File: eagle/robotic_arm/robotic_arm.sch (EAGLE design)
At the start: 0 parts

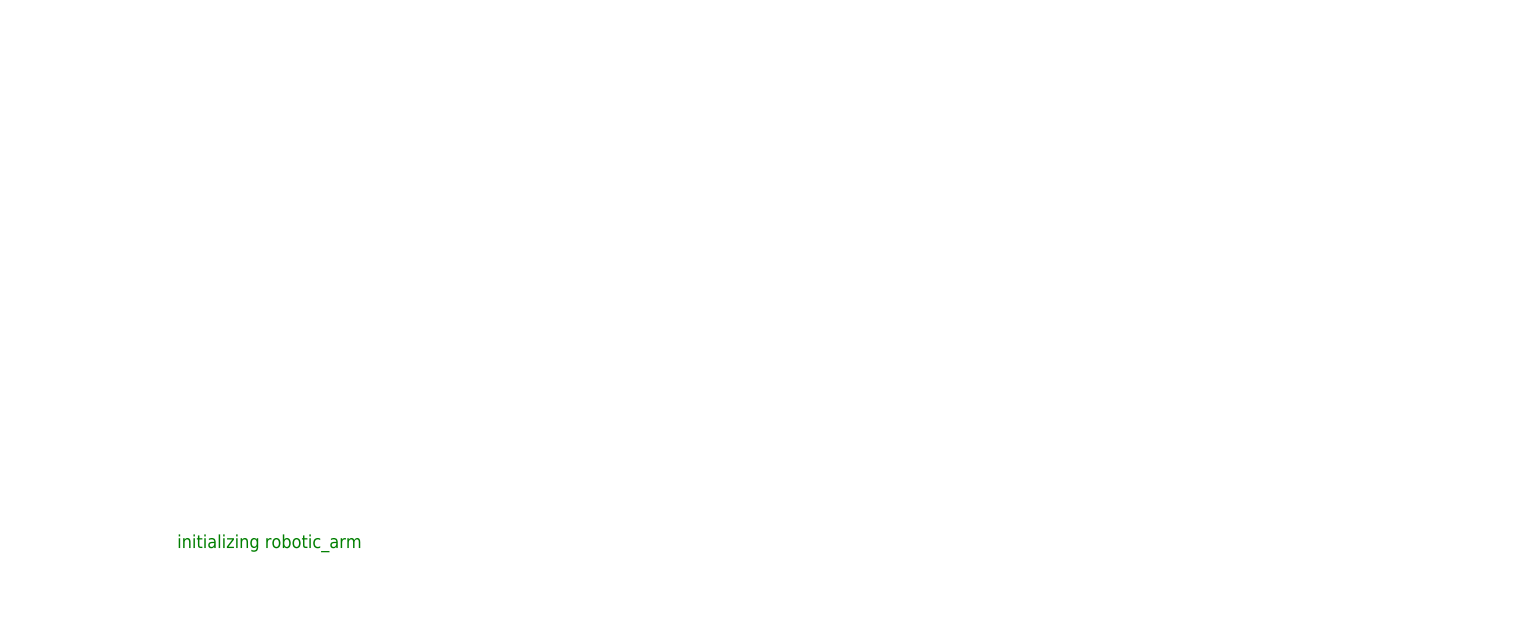
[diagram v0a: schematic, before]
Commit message: Added PWM driver and DEMUX to both robotic arm and touch glove.  Added some transistors to touch glove
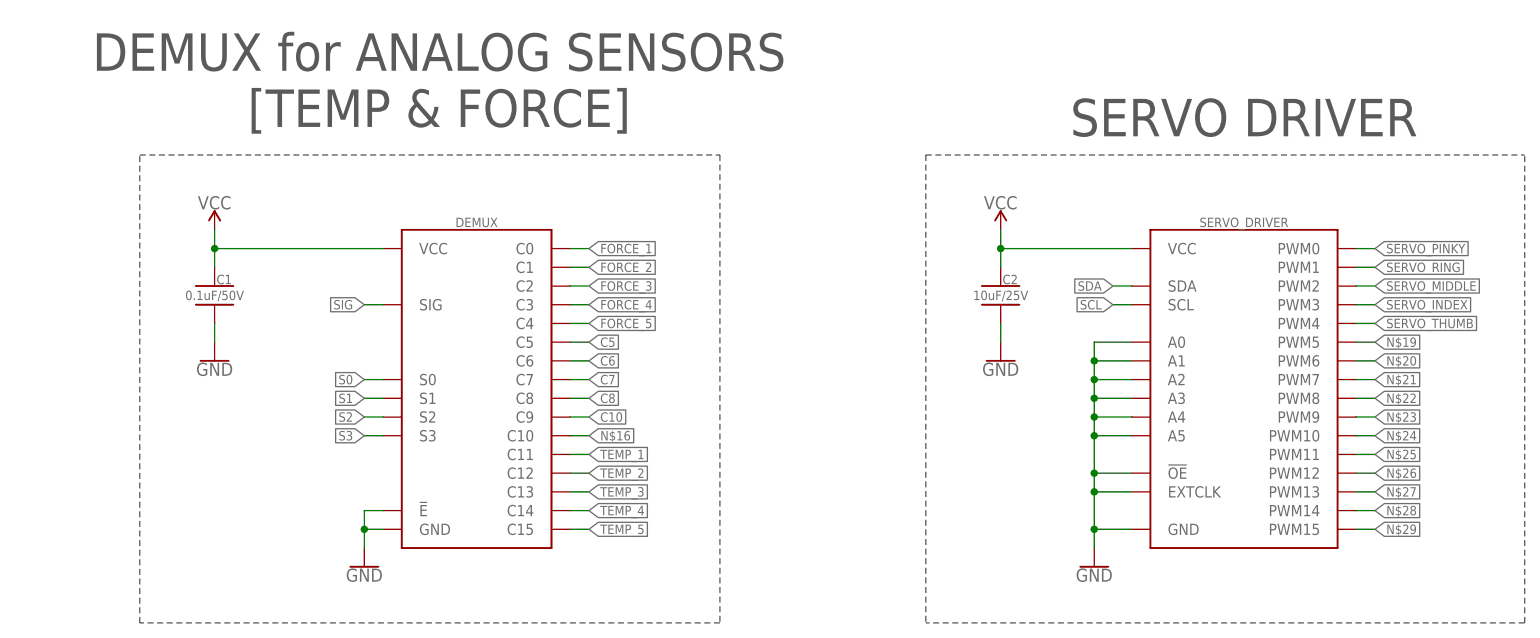
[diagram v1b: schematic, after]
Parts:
- added C1: CAP_CER_SMD-805_0.1UF-50V-10%, MrSwirlyEyes:CAP_CER_SMD-805_0.1UF-50V-10%
- added C2: CAP_CER_SMD-805_10UF-25V-10%, MrSwirlyEyes:CAP_CER_SMD-805_10UF-25V-10%
- added DEMUX: CD74HCT4067_16-CH_MUX-DEMUX, MrSwirlyEyes:CD74HCT4067_16-CH_MUX-DEMUX
- added SERVO_DRIVER: PCA9685_16-CH_12-BIT_PWM-DRIVER, MrSwirlyEyes:PCA9685_16-CH_12-BIT_PWM-DRIVER
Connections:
- new net C10: DEMUX.C9
- new net C5: DEMUX.C5
- new net C6: DEMUX.C6
- new net C7: DEMUX.C7
- new net C8: DEMUX.C8
- new net FORCE_1: DEMUX.C0
- new net FORCE_2: DEMUX.C1
- new net FORCE_3: DEMUX.C2
- new net FORCE_4: DEMUX.C3
- new net FORCE_5: DEMUX.C4
- new net GND: C1.2, C2.2, DEMUX.!E, DEMUX.GND, SERVO_DRIVER.!OE, SERVO_DRIVER.A0, SERVO_DRIVER.A1, SERVO_DRIVER.A2, SERVO_DRIVER.A3, SERVO_DRIVER.A4, SERVO_DRIVER.A5, SERVO_DRIVER.EXTCLK, SERVO_DRIVER.GND
- new net N$16: DEMUX.C10
- new net N$19: SERVO_DRIVER.PWM5
- new net N$20: SERVO_DRIVER.PWM6
- new net N$21: SERVO_DRIVER.PWM7
- new net N$22: SERVO_DRIVER.PWM8
- new net N$23: SERVO_DRIVER.PWM9
- new net N$24: SERVO_DRIVER.PWM10
- new net N$25: SERVO_DRIVER.PWM11
- new net N$26: SERVO_DRIVER.PWM12
- new net N$27: SERVO_DRIVER.PWM13
- new net N$28: SERVO_DRIVER.PWM14
- new net N$29: SERVO_DRIVER.PWM15
- new net S0: DEMUX.S0
- new net S1: DEMUX.S1
- new net S2: DEMUX.S2
- new net S3: DEMUX.S3
- new net SCL: SERVO_DRIVER.SCL
- new net SDA: SERVO_DRIVER.SDA
- new net SERVO_INDEX: SERVO_DRIVER.PWM3
- new net SERVO_MIDDLE: SERVO_DRIVER.PWM2
- new net SERVO_PINKY: SERVO_DRIVER.PWM0
- new net SERVO_RING: SERVO_DRIVER.PWM1
- new net SERVO_THUMB: SERVO_DRIVER.PWM4
- new net SIG: DEMUX.SIG
- new net TEMP_1: DEMUX.C11
- new net TEMP_2: DEMUX.C12
- new net TEMP_3: DEMUX.C13
- new net TEMP_4: DEMUX.C14
- new net TEMP_5: DEMUX.C15
- new net VCC: C1.1, C2.1, DEMUX.VCC, SERVO_DRIVER.VCC
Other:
- note added: "DEMUX for ANALOG SENSORS [TEMP & FORCE]"
- note added: "SERVO DRIVER"
- note removed: "initializing robotic_arm"

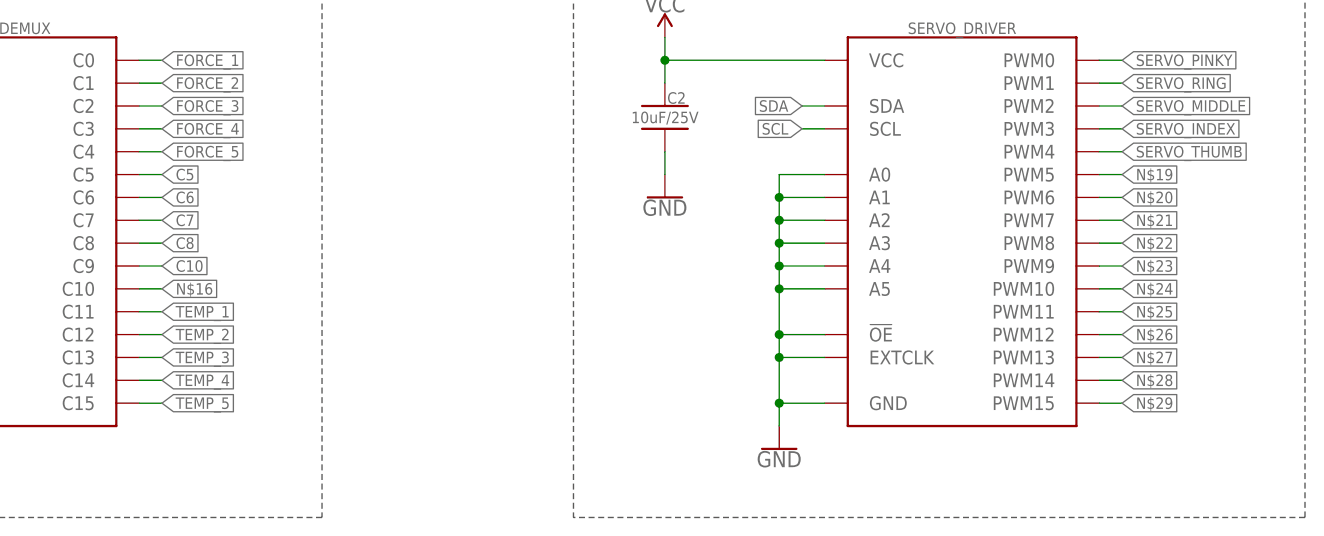
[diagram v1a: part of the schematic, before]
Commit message: Added vibe motor plus transistor driver arrangement
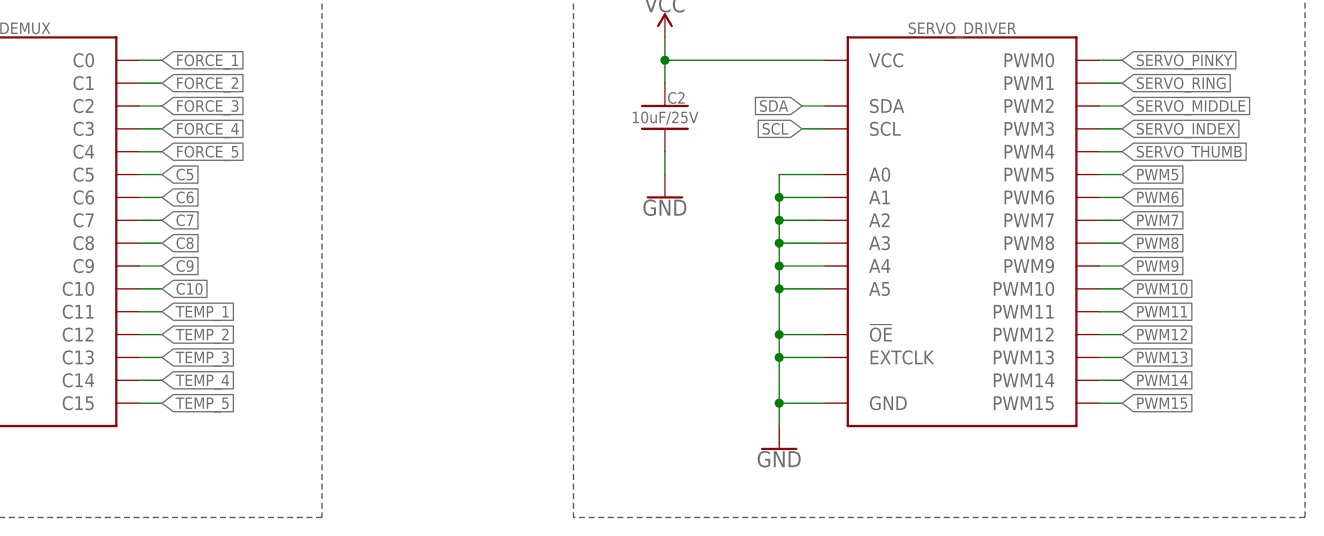
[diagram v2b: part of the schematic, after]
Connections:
- net N$19 renamed PWM5
- net N$20 renamed PWM6
- net N$21 renamed PWM7
- net N$22 renamed PWM8
- net N$23 renamed PWM9
- net N$24 renamed PWM10
- net N$25 renamed PWM11
- net N$26 renamed PWM12
- net N$27 renamed PWM13
- net N$28 renamed PWM14
- net N$29 renamed PWM15
- removed net N$16: DEMUX.C10
- new net C9: DEMUX.C9
- net C10: now also DEMUX.C10; no longer DEMUX.C9
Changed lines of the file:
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@@
 </segment>
 </net>
-<net name="C10" class="0">
+<net name="C9" class="0">
 <segment>
 <pinref part="DEMUX" gate="G$1" pin="C9"/>
@@
 </segment>
 </net>
-<net name="N$16" class="0">
+<net name="C10" class="0">
 <segment>
 <pinref part="DEMUX" gate="G$1" pin="C10"/>
@@
 </segment>
 </net>
-<net name="N$19" class="0">
+<net name="PWM5" class="0">
 <segment>
 <pinref part="SERVO_DRIVER" gate="G$1" pin="PWM5"/>
@@
 </segment>
 </net>
-<net name="N$20" class="0">
+<net name="PWM6" class="0">
 <segment>
 <pinref part="SERVO_DRIVER" gate="G$1" pin="PWM6"/>
@@
 </segment>
 </net>
-<net name="N$21" class="0">
+<net name="PWM7" class="0">
 <segment>
 <pinref part="SERVO_DRIVER" gate="G$1" pin="PWM7"/>
@@
 </segment>
 </net>
-<net name="N$22" class="0">
+<net name="PWM8" class="0">
 <segment>
 <pinref part="SERVO_DRIVER" gate="G$1" pin="PWM8"/>
@@
 </segment>
 </net>
-<net name="N$23" class="0">
+<net name="PWM9" class="0">
 <segment>
 <pinref part="SERVO_DRIVER" gate="G$1" pin="PWM9"/>
@@
 </segment>
 </net>
-<net name="N$24" class="0">
+<net name="PWM10" class="0">
 <segment>
 <pinref part="SERVO_DRIVER" gate="G$1" pin="PWM10"/>
@@
 </segment>
 </net>
-<net name="N$25" class="0">
+<net name="PWM11" class="0">
 <segment>
 <pinref part="SERVO_DRIVER" gate="G$1" pin="PWM11"/>
@@
 </segment>
 </net>
-<net name="N$26" class="0">
+<net name="PWM12" class="0">
 <segment>
 <pinref part="SERVO_DRIVER" gate="G$1" pin="PWM12"/>
@@
 </segment>
 </net>
-<net name="N$27" class="0">
+<net name="PWM13" class="0">
 <segment>
 <pinref part="SERVO_DRIVER" gate="G$1" pin="PWM13"/>
@@
 </segment>
 </net>
-<net name="N$28" class="0">
+<net name="PWM14" class="0">
 <segment>
 <pinref part="SERVO_DRIVER" gate="G$1" pin="PWM14"/>
@@
 </segment>
 </net>
-<net name="N$29" class="0">
+<net name="PWM15" class="0">
 <segment>
 <pinref part="SERVO_DRIVER" gate="G$1" pin="PWM15"/>

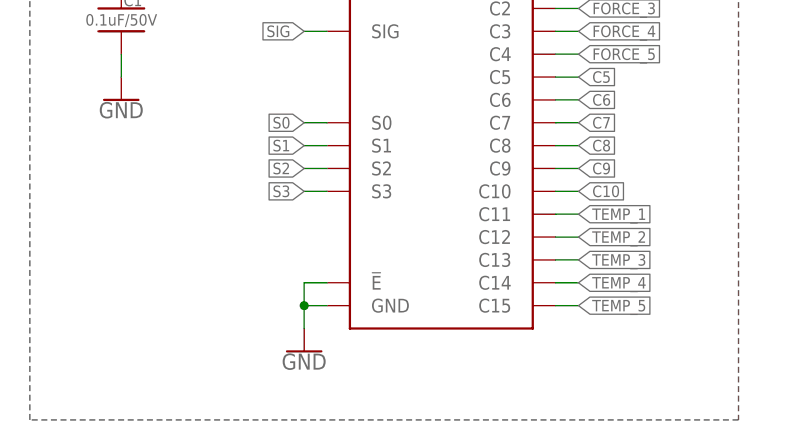
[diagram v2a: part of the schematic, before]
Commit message: Added Peltier driving circuitry
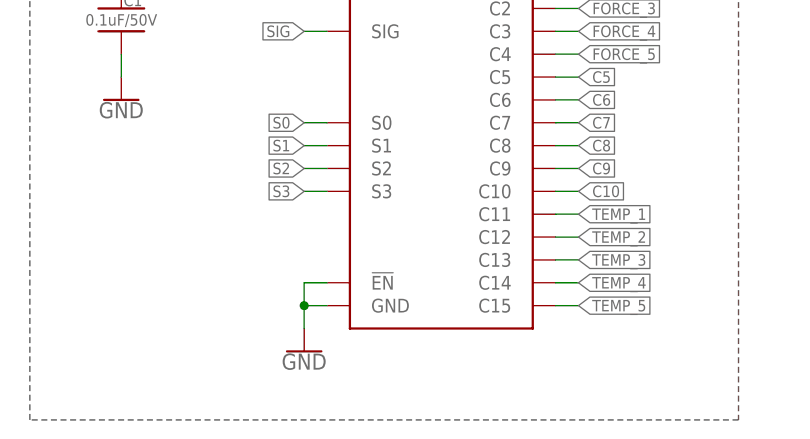
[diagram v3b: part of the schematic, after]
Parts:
- DEMUX: value CD74HCT4067_16-CH_MUX-DEMUX -> CD74HC4067-SM96_16:1_MUX-DEMUX; device MrSwirlyEyes:CD74HCT4067_16-CH_MUX-DEMUX -> MrSwirlyEyes:CD74HC4067-SM96_16:1_MUX-DEMUX
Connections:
- net GND: now also DEMUX.!EN; no longer DEMUX.!E
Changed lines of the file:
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@@
 </classes>
 <parts>
-<part name="DEMUX" library="MrSwirlyEyes" deviceset="CD74HCT4067_16-CH_MUX-DEMUX" device=""/>
+<part name="DEMUX" library="MrSwirlyEyes" deviceset="CD74HC4067-SM96_16:1_MUX-DEMUX" device=""/>
 <part name="C1" library="MrSwirlyEyes" deviceset="CAP_CER_SMD-805_0.1UF-50V-10%" device=""/>
 <part name="GND1" library="SparkFun-PowerSymbols" deviceset="GND" device=""/>
@@
 <net name="GND" class="0">
 <segment>
-<pinref part="DEMUX" gate="G$1" pin="!E"/>
+<pinref part="DEMUX" gate="G$1" pin="!EN"/>
 <wire x1="35.56" y1="17.78" x2="33.02" y2="17.78" width="0.1524" layer="91"/>
 <wire x1="33.02" y1="17.78" x2="33.02" y2="15.24" width="0.1524" layer="91"/>

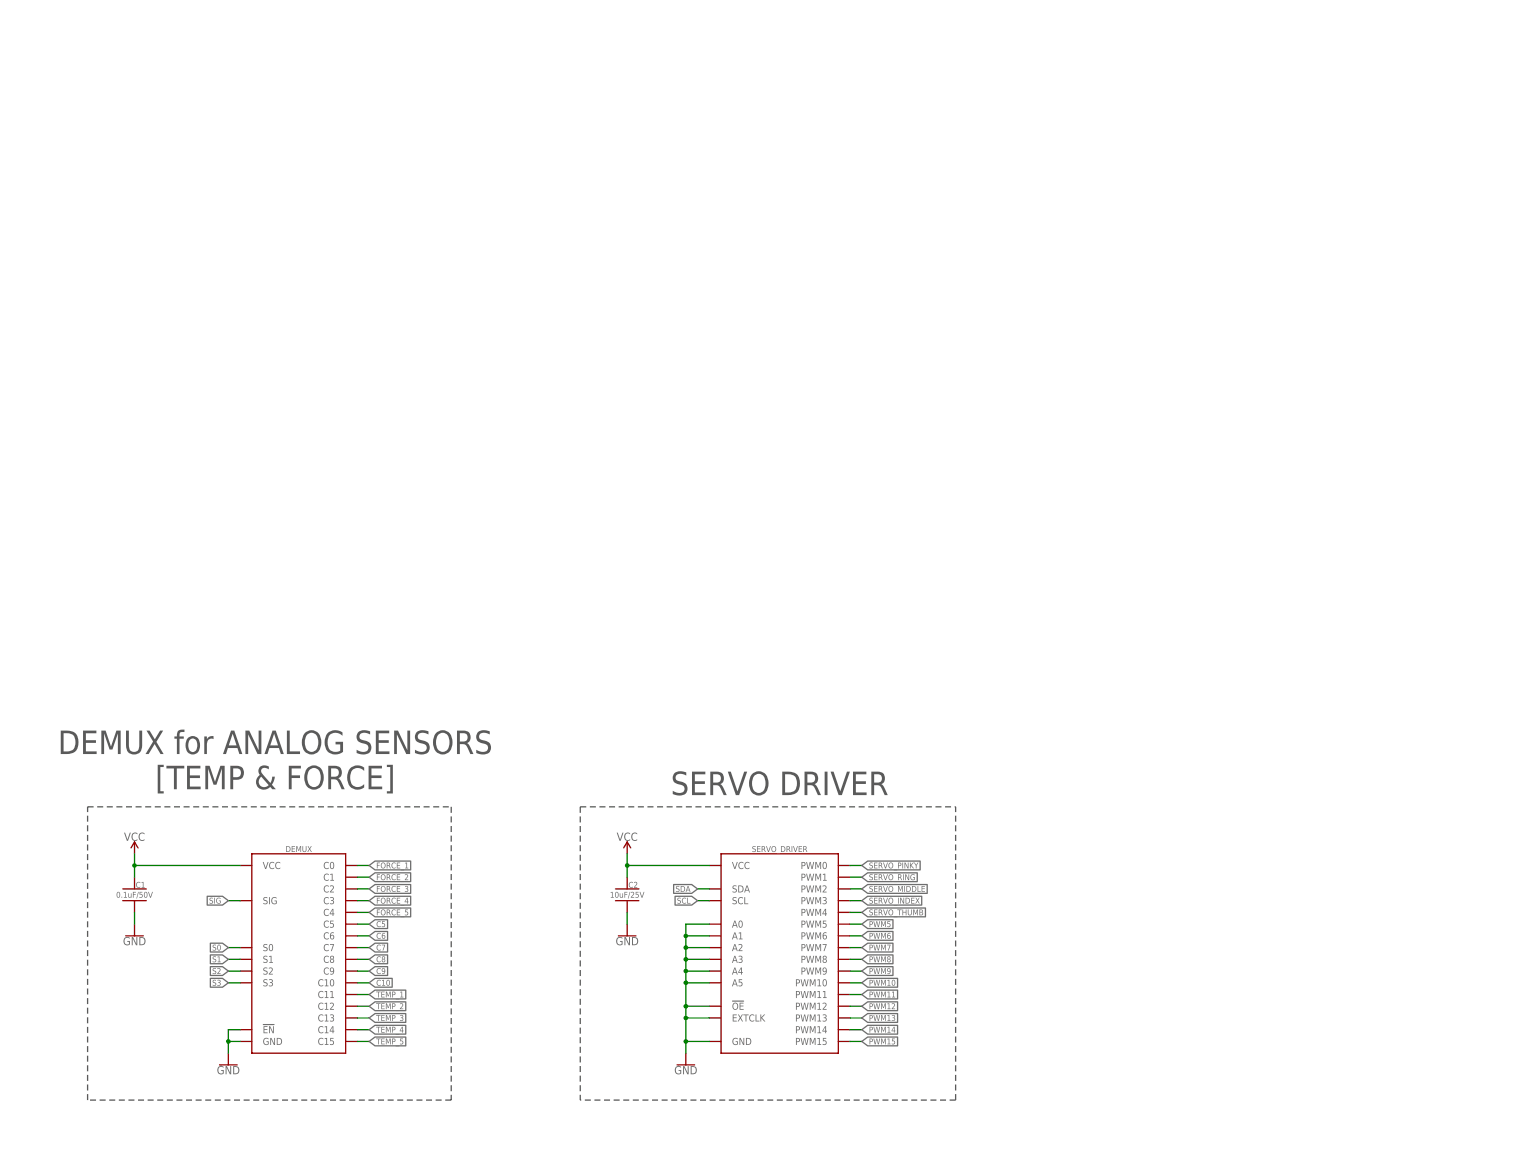
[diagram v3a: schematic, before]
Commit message: Added FSR driver and servo driver for robotic arm
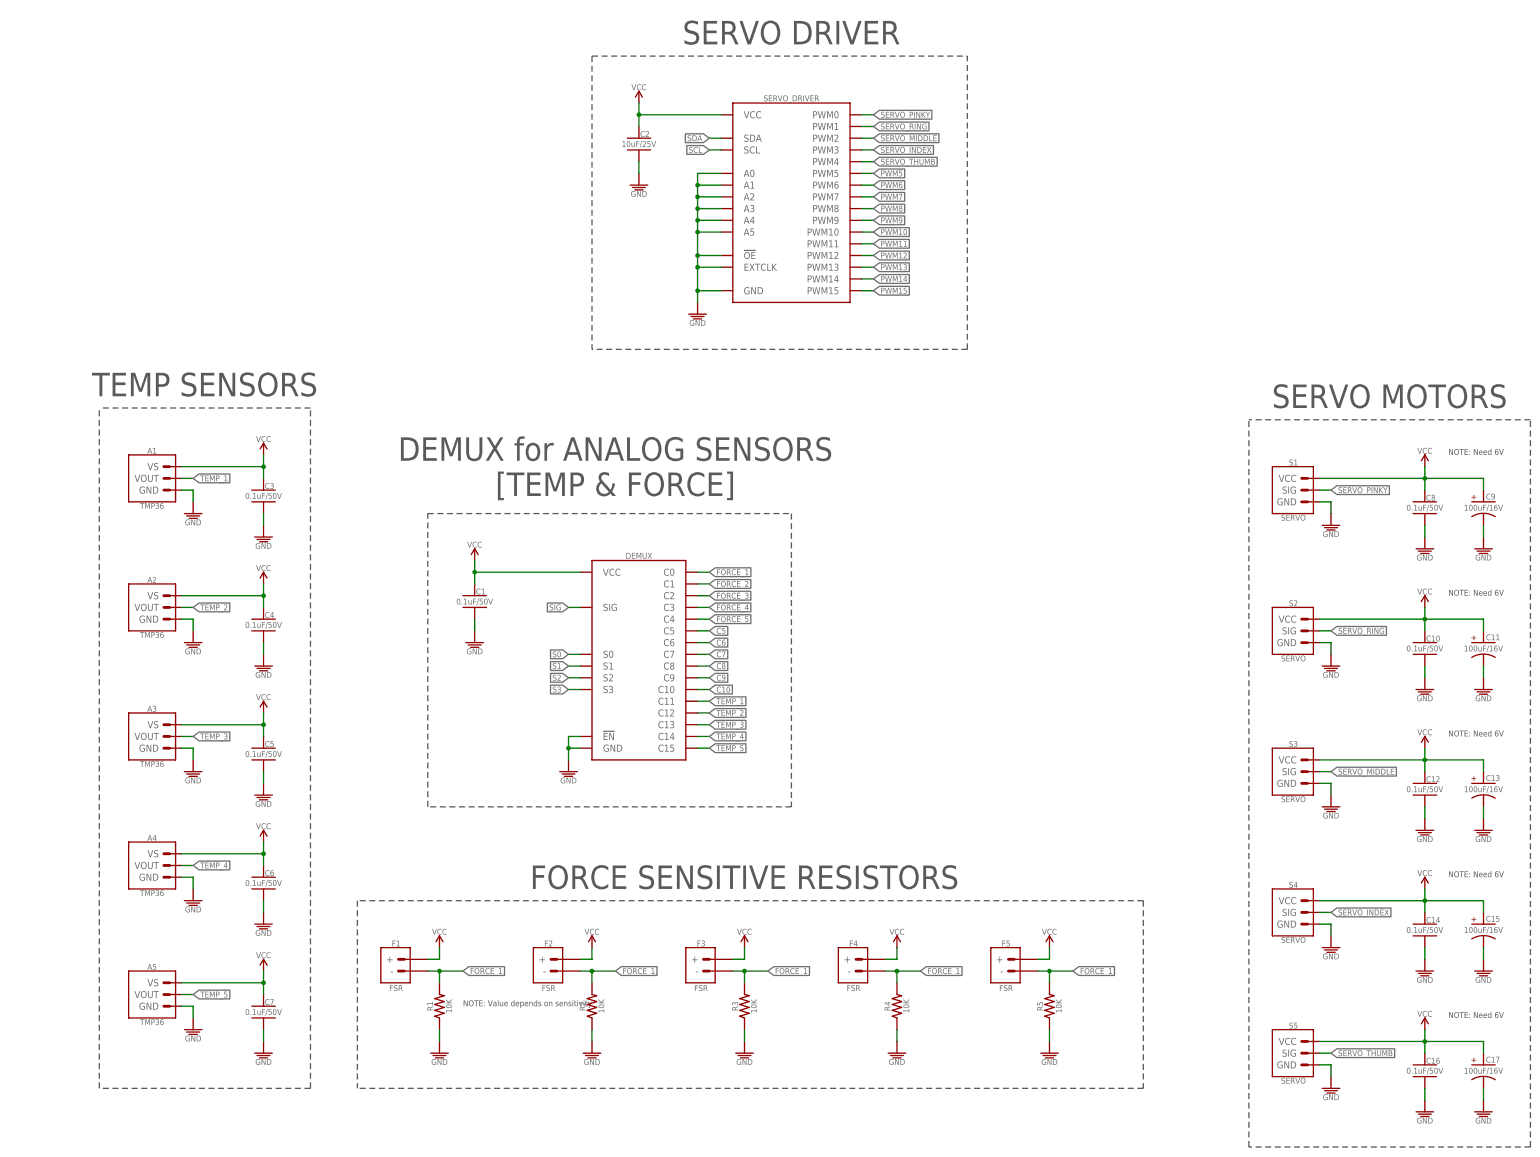
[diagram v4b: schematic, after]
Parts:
- added A1, A2, A3, A4, A5: TMP36, MrSwirlyEyes:TMP36
- added C10, C12, C14, C16, C3, C4, C5, C6, C7, C8: CAP_CER_SMD-805_0.1UF-50V-10%, MrSwirlyEyes:CAP_CER_SMD-805_0.1UF-50V-10%
- added C11, C13, C15, C17, C9: CAP_POL_ALUM-ELECTROLYTIC_SMD_100UF-16V-20%, MrSwirlyEyes:CAP_POL_ALUM-ELECTROLYTIC_SMD_100UF-16V-20%
- added F1, F2, F3, F4, F5: FSR, MrSwirlyEyes:FSR
- added R1, R2, R3, R4, R5: RES_SMD-805_10K-5%-1/8W, MrSwirlyEyes:RES_SMD-805_10K-5%-1/8W
- added S1, S2, S3, S4, S5: SERVO, MrSwirlyEyes:SERVO
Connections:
- net FORCE_1: now also F1.-, F2.-, F3.-, F4.-, F5.-, R1.2, R2.2, R3.2, R4.2, R5.2
- net GND: now also A1.GND, A2.GND, A3.GND, A4.GND, A5.GND, C10.2, C11.K, C12.2, C13.K, C14.2, C15.K, C16.2, C17.K, C3.2, C4.2, C5.2, C6.2, C7.2, C8.2, C9.K, R1.1, R2.1, R3.1, R4.1, R5.1, S1.GND, S2.GND, S3.GND, S4.GND, S5.GND
- net SERVO_INDEX: now also S4.SIG
- net SERVO_MIDDLE: now also S3.SIG
- net SERVO_PINKY: now also S1.SIG
- net SERVO_RING: now also S2.SIG
- net SERVO_THUMB: now also S5.SIG
- net TEMP_1: now also A1.VOUT
- net TEMP_2: now also A2.VOUT
- net TEMP_3: now also A3.VOUT
- net TEMP_4: now also A4.VOUT
- net TEMP_5: now also A5.VOUT
- net VCC: now also A1.VS, A2.VS, A3.VS, A4.VS, A5.VS, C10.1, C11.A, C12.1, C13.A, C14.1, C15.A, C16.1, C17.A, C3.1, C4.1, C5.1, C6.1, C7.1, C8.1, C9.A, F1.+, F2.+, F3.+, F4.+, F5.+, S1.VCC, S2.VCC, S3.VCC, S4.VCC, S5.VCC
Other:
- note added: "FORCE SENSITIVE RESISTORS"
- note added: "NOTE: Need 6V"
- note added: "NOTE: Value depends on sensitivity"
- note added: "SERVO MOTORS"
- note added: "TEMP SENSORS"
- moved on the sheet: C1, C2, DEMUX, SERVO_DRIVER
